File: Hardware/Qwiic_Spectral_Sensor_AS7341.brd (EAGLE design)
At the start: 25.4 x 25.4 mm, 58 parts, among them J1 QWIIC_RIGHT_ANGLE, J3 QWIIC_RIGHT_ANGLE, Q1 20V/4.2A/52mΩ/1.4W, Q2 20V/4.2A/52mΩ/1.4W, Q3 20V/4.2A/52mΩ/1.4W, U1 AS7341OLGA, U2 PCA9536, U3 AP2127K-1.8V

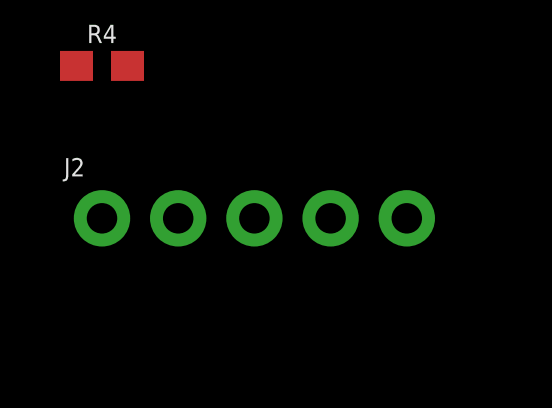
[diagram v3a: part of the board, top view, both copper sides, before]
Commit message: added as7341 decoupling cap
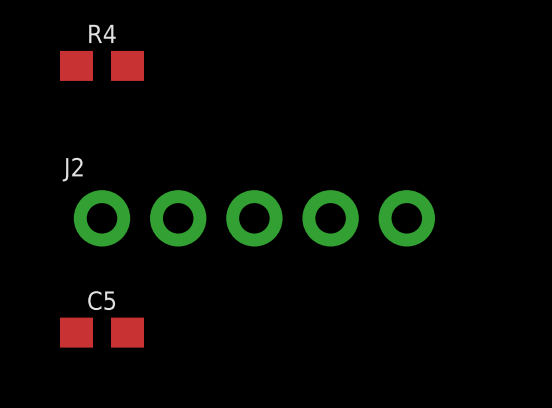
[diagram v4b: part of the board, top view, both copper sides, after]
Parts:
- added C5: 0.1uF, SparkFun-Capacitors:0603
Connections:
- net 1.8V: now also C5.1
- net GND: now also C5.2
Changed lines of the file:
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@@
 <attribute name="VALUE" x="-50.8" y="-75.692" size="0.6096" layer="27" font="vector" ratio="20"/>
+</element>
+<element name="C5" library="SparkFun-Capacitors" package="0603" value="0.1uF" x="-49.53" y="-77.47" smashed="yes">
+<attribute name="NAME" x="-49.53" y="-76.708" size="0.6096" layer="25" font="vector" ratio="20" align="bottom-center"/>
+<attribute name="PROD_ID" value="CAP-00810" x="-49.53" y="-77.47" size="1.778" layer="27" font="vector" ratio="15" display="off"/>
+<attribute name="VALUE" x="-49.53" y="-78.232" size="0.6096" layer="27" font="vector" ratio="20" align="top-center"/>
 </element>
 </elements>
@@
 <contactref element="C4" pad="2"/>
 <contactref element="J2" pad="1"/>
+<contactref element="C5" pad="2"/>
+<wire x1="-49.53" y1="-73.66" x2="-48.68" y2="-77.47" width="0" layer="19" extent="1-1"/>
 <wire x1="-18.2" y1="-34.29" x2="-49.53" y2="-73.66" width="0" layer="19" extent="1-1"/>
 <wire x1="-18.2" y1="-30.48" x2="-18.2" y2="-34.29" width="0" layer="19" extent="1-1"/>
@@
 <contactref element="C4" pad="1"/>
 <contactref element="R4" pad="2"/>
+<contactref element="C5" pad="1"/>
+<wire x1="-48.68" y1="-68.58" x2="-50.38" y2="-77.47" width="0" layer="19" extent="1-1"/>
 <wire x1="-19.9" y1="-34.29" x2="-48.68" y2="-68.58" width="0" layer="19" extent="1-1"/>
 <wire x1="-20" y1="-22.8299" x2="-19.9" y2="-34.29" width="0" layer="19" extent="1-1"/>

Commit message: Board design
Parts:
- removed U$11, U$5: (no value), output:IR0
- removed U$21, U$22: (no value), output:THERMOMETER0
- removed U$23, U$24: (no value), output:MLX906140
- removed U$3, U$4: (no value), output:QWIIC0
- J2: device SparkFun-Connectors:1X05_NO_SILK -> SparkFun-Connectors:1X06_NO_SILK
- moved C5 118.0 mm to (16.5, 20.3)
- moved R4 111.1 mm to (20.3, 17.8), turned to 90 degrees
- moved Q3 100.0 mm to (6.35, 22.9), turned to 180 degrees
- moved J2 95.8 mm to (10.2, 1.27)
- moved Q2 95.3 mm to (22.9, 10.2)
- moved JP3 82.6 mm to (24.1, 17.8), flipped to the bottom, turned to 270 degrees
- moved Q1 80.8 mm to (10.2, 10.2)
- moved JP4 79.1 mm to (8.89, 17.8), flipped to the bottom, turned to 270 degrees
- moved D5 73.7 mm to (21.6, 14.0), turned to 90 degrees
- moved D3 73.3 mm to (21.6, 19.1), turned to 270 degrees
- moved C4 68.2 mm to (14.0, 25.4), turned to 270 degrees
- moved C3 67.6 mm to (19.1, 25.4), turned to 90 degrees
- moved D2 64.8 mm to (11.4, 19.1), turned to 270 degrees
- moved R2 64.3 mm to (25.4, 24.1), turned to 180 degrees
- moved D4 64.1 mm to (11.4, 14.0), turned to 90 degrees
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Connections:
- net INT renamed !INT!
- removed net N$6: U3.1, U3.3
- net 3.3V: now also Q1.2, Q2.2, U3.1, U3.3; no longer Q1.3, Q2.3
- net GPIO3: now also J2.6, U1.6
- net N$8: now also Q1.3; no longer Q1.2
- net N$9: now also Q2.3; no longer Q2.2
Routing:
- net 3.3V: track 21.6 -> 83.1 mm, vias 2 -> 1
- net SDA: track 16.9 -> 66.5 mm, vias 1 -> 3
- net LDR: track 0.00 -> 20.9 mm, vias 0 -> 1
- net !INT!: track 0.00 -> 20.9 mm, vias 0 -> 1
- net GPIO3: track 0.00 -> 20.1 mm, vias 0 -> 2
- net 1.8V: track 0.00 -> 19.9 mm, vias 0 -> 1
- net GPIO0: track 0.00 -> 19.4 mm, vias 0 -> 2
- net SCL: track 34.4 -> 53.3 mm, vias 1 -> 3
- net GPIO2: track 0.00 -> 8.99 mm, vias 0 -> 2
- net N$9: track 0.00 -> 8.82 mm
- net N$8: track 0.00 -> 8.74 mm
- net GPIO1: track 0.00 -> 6.00 mm
- net N$5: track 0.00 -> 4.16 mm, vias 0 -> 1
- net N$7: track 0.00 -> 3.89 mm, vias 0 -> 1
- net N$10: track 0.00 -> 3.45 mm, vias 0 -> 1
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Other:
- board size 25.4 x 25.4 mm -> 31.8 x 31.8 mm

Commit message: Update Qwiic_Spectral_Sensor_AS7341.brd
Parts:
- moved U$7 36.7 mm to (5.08, 7.62)
- moved U$6 34.9 mm to (5.08, 7.62)
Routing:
- net 3.3V: track 83.1 -> 93.7 mm, vias 1 -> 2
- net 1.8V: track 19.9 -> 22.9 mm, vias 1 -> 2
- net GND: vias 8 -> 9
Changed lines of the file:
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@@
 <element name="U$19" library="output" package="#SCL#0" value="" x="17.78" y="1.651" smashed="yes" rot="R90"/>
 <element name="U$20" library="output" package="#SCL#0" value="" x="17.78" y="1.651" smashed="yes" rot="MR90"/>
-<element name="U$6" library="SparkX" package="SPARKX-SMALL" value="" x="39.37" y="13.97" smashed="yes"/>
-<element name="U$7" library="SparkX" package="SPARKX-SMALL" value="" x="40.64" y="16.51" smashed="yes" rot="MR0"/>
+<element name="U$6" library="SparkX" package="SPARKX-SMALL" value="" x="5.08" y="7.62" smashed="yes"/>
+<element name="U$7" library="SparkX" package="SPARKX-SMALL" value="" x="5.08" y="7.62" smashed="yes" rot="MR0"/>
 <element name="U1" library="AS7341" package="OLGA8" value="AS7341OLGA" x="16.51" y="16.51" smashed="yes" rot="R270">
 <attribute name="NAME" x="14.478" y="18.161" size="0.635" layer="25" font="vector" rot="R270"/>
@@
 <wire x1="8.5946625" y1="22.2504" x2="16.2814" y2="22.2504" width="0.2032" layer="1"/>
 <wire x1="16.51" y1="22.479" x2="16.51" y2="22.987" width="0.2032" layer="1"/>
-<wire x1="16.09" y1="7.62" x2="18.76" y2="11.135" width="0" layer="19" extent="1-1"/>
+<wire x1="19.05" y1="24.55" x2="20.105" y2="24.55" width="0.2032" layer="1"/>
+<wire x1="20.105" y1="24.55" x2="20.193" y2="24.638" width="0.2032" layer="1"/>
+<via x="20.193" y="24.638" extent="1-16" drill="0.508"/>
+<wire x1="20.193" y1="24.638" x2="20.955" y2="25.4" width="0.2032" layer="16"/>
+<wire x1="20.955" y1="25.4" x2="29.21" y2="25.4" width="0.2032" layer="16"/>
 </signal>
 <signal name="SDA">
@@
 <contactref element="R2" pad="2"/>
 <wire x1="5.08" y1="15.01" x2="9.295" y2="15.01" width="0.2032" layer="1"/>
-<wire x1="11.195" y1="16.91" x2="15.872" y2="16.91" width="0.2032" layer="1"/>
-<wire x1="9.295" y1="15.01" x2="11.195" y2="16.91" width="0.2032" layer="1"/>
+<wire x1="11.195" y1="16.91" x2="9.295" y2="15.01" width="0.2032" layer="1"/>
 <contactref element="J2" pad="4"/>
 <wire x1="18.76" y1="9.835" x2="17.78" y2="9.835" width="0.2032" layer="1"/>
@@
 <via x="24.55" y="22.86" extent="1-16" drill="0.508"/>
 <wire x1="15.0368" y1="21.8948" x2="16.002" y2="22.86" width="0.2032" layer="16"/>
-<wire x1="13.6017375" y1="16.8972625" x2="15.872" y2="16.91" width="0" layer="19" extent="1-1"/>
+<wire x1="13.6017375" y1="16.8972625" x2="14.2237875" y2="16.8972625" width="0.2032" layer="1"/>
+<wire x1="14.2237875" y1="16.8972625" x2="14.268325" y2="16.9418" width="0.2032" layer="1"/>
+<wire x1="14.268325" y1="16.9418" x2="14.941675" y2="16.9418" width="0.2032" layer="1"/>
+<wire x1="14.941675" y1="16.9418" x2="14.973475" y2="16.91" width="0.2032" layer="1"/>
+<wire x1="14.973475" y1="16.91" x2="15.872" y2="16.91" width="0.2032" layer="1"/>
+<wire x1="13.6017375" y1="16.8972625" x2="11.2077375" y2="16.8972625" width="0.2032" layer="1"/>
+<wire x1="11.2077375" y1="16.8972625" x2="11.195" y2="16.91" width="0.2032" layer="1"/>
 </signal>
 <signal name="N$2">
@@
 <via x="14.605" y="16.129" extent="1-16" drill="0.508"/>
 <via x="12.7" y="8.89" extent="1-16" drill="0.508"/>
-<wire x1="15.872" y1="16.11" x2="17.148" y2="15.31" width="0" layer="19" extent="1-1"/>
+<via x="17.78" y="14.351" extent="1-16" drill="0.508"/>
 </signal>
 <signal name="N$4">
@@
 <via x="14.224" y="20.955" extent="1-16" drill="0.508"/>
 <wire x1="14.224" y1="20.955" x2="14.224" y2="22.733" width="0.2032" layer="16"/>
-<wire x1="14.224" y1="22.733" x2="13.081" y2="23.876" width="0.2032" layer="16"/>
-<wire x1="13.081" y1="23.876" x2="13.081" y2="26.289" width="0.2032" layer="16"/>
-<wire x1="13.081" y1="26.289" x2="13.97" y2="26.25" width="0" layer="19" extent="1-16"/>
+<wire x1="13.081" y1="23.876" x2="14.224" y2="22.733" width="0.2032" layer="16"/>
+<wire x1="13.97" y1="26.25" x2="13.97" y2="27.559" width="0.2032" layer="1"/>
+<via x="13.97" y="27.559" extent="1-16" drill="0.508"/>
+<wire x1="13.97" y1="27.559" x2="13.081" y2="26.67" width="0.2032" layer="16"/>
+<wire x1="13.081" y1="26.67" x2="13.081" y2="23.876" width="0.2032" layer="16"/>
 </signal>
 <signal name="LDR">
@@
 <wire x1="11.487" y1="15.31" x2="11.43" y2="15.367" width="0.2032" layer="1"/>
 <wire x1="21.59" y1="15.24" x2="21.59" y2="18.173" width="0.2032" layer="1"/>
-<wire x1="21.59" y1="15.24" x2="20.32" y2="13.97" width="0.2032" layer="1"/>
-<wire x1="14.732" y1="13.97" x2="14.478" y2="14.224" width="0.2032" layer="1"/>
-<wire x1="14.478" y1="14.224" x2="14.478" y2="15.31" width="0.2032" layer="1"/>
-<wire x1="20.32" y1="13.97" x2="14.732" y2="13.97" width="0.2032" layer="1"/>
+<wire x1="14.478" y1="15.31" x2="14.478" y2="14.224" width="0.2032" layer="1"/>
 <wire x1="11.43" y1="18.223" x2="12.511" y2="18.223" width="0.2032" layer="1"/>
 <via x="12.573" y="18.161" extent="1-16" drill="0.508"/>
@@
 <wire x1="11.43" y1="16.383" x2="11.43" y2="15.24" width="0.2032" layer="16"/>
 <wire x1="12.511" y1="18.223" x2="12.573" y2="18.161" width="0.2032" layer="1"/>
+<wire x1="14.478" y1="14.224" x2="14.8082" y2="13.8938" width="0.2032" layer="1"/>
+<wire x1="15.830675" y1="13.8938" x2="16.219675" y2="13.5048" width="0.2032" layer="1"/>
+<wire x1="14.8082" y1="13.8938" x2="15.830675" y2="13.8938" width="0.2032" layer="1"/>
+<wire x1="16.219675" y1="13.5048" x2="19.8548" y2="13.5048" width="0.2032" layer="1"/>
+<wire x1="19.8548" y1="13.5048" x2="21.59" y2="15.24" width="0.2032" layer="1"/>
 </signal>
 <signal name="N$5">
@@
 <mfgpreviewcolor name="substratecolor" color="0xFF786E46"/>
 </mfgpreviewcolors>
-<errors>
-</errors>
 </board>
 </drawing>

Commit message: Update Qwiic_Spectral_Sensor_AS7341.brd
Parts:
- moved R1 1.27 mm to (25.4, 25.4)
- moved JP1 1.27 mm to (29.2, 24.1)
- moved R2 1.27 mm to (25.4, 22.9)
- moved U$9 1.27 mm to (28.4, 24.1)
- moved FD2 0.18 mm to (30.6, 26.8)
- moved FD4 0.18 mm to (30.6, 26.8)
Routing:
- net SDA: track 66.5 -> 64.1 mm
- net 3.3V: track 93.7 -> 92.3 mm
- net SCL: track 53.4 -> 52.2 mm
- net GPIO2: track 8.99 -> 9.98 mm

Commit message: Buzzard labels
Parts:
- added U$11, U$21: (no value), output:SENSOR0
- added U$22, U$23: (no value), output:AS73410
- added U$24, U$25: (no value), output:#GPIO#0
- added U$26, U$27: (no value), output:##INT##0
- added U$3, U$4: (no value), output:QWIIC0
- added U$5, U$8: (no value), output:SPECTRAL0
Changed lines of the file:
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@@
 <?xml version="1.0" encoding="utf-8"?>
 <!DOCTYPE eagle SYSTEM "eagle.dtd">
-<eagle version="9.5.2">
+<eagle version="9.6.2">
 <drawing>
 <settings>
-<setting alwaysvectorfont="yes"/>
+<setting alwaysvectorfont="no"/>
 <setting keepoldvectorfont="yes"/>
 <setting verticaltext="up"/>
@@
 <attribute name="VALUE" x="8.89" y="-0.762" size="0.6096" layer="27" font="vector" ratio="20"/>
 </element>
+<element name="U$3" library="output" package="QWIIC0" value="" x="6.35" y="30.48" smashed="yes"/>
+<element name="U$4" library="output" package="QWIIC0" value="" x="11.43" y="35.56" smashed="yes" rot="MR0"/>
+<element name="U$5" library="output" package="SPECTRAL0" value="" x="12.7" y="30.48" smashed="yes"/>
+<element name="U$8" library="output" package="SPECTRAL0" value="" x="20.32" y="35.56" smashed="yes" rot="MR0"/>
+<element name="U$11" library="output" package="SENSOR0" value="" x="20.32" y="30.48" smashed="yes"/>
+<element name="U$21" library="output" package="SENSOR0" value="" x="27.94" y="35.56" smashed="yes" rot="MR0"/>
+<element name="U$22" library="output" package="AS73410" value="" x="12.7" y="29.21" smashed="yes"/>
+<element name="U$23" library="output" package="AS73410" value="" x="19.05" y="33.02" smashed="yes" rot="MR0"/>
+<element name="U$24" library="output" package="#GPIO#0" value="" x="22.86" y="1.778" smashed="yes" rot="R90"/>
+<element name="U$25" library="output" package="#GPIO#0" value="" x="22.86" y="1.778" smashed="yes" rot="MR90"/>
+<element name="U$26" library="output" package="##INT##0" value="" x="20.32" y="1.778" smashed="yes" rot="R90"/>
+<element name="U$27" library="output" package="##INT##0" value="" x="20.32" y="1.778" smashed="yes" rot="MR90"/>
 </elements>
 <signals>
